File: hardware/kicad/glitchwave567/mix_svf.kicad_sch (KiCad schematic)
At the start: 50 parts, among them Q4 MMBT3904, Q5 MMBT3904, Q6 MMBT3904, U10 LM13700, U11 LM13700, U12 LM13700, U13 CD4051B, U9 TL074

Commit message: hardware: root hierarchy + ERC pass on KiCad 10 (down to lib-mismatch/footprint noise + 2 intentional OTA current-sum waivers)
- root sheet ties all 8 sheets into one project (global-label connectivity, 288 comps / 259 nets stitch verified)
- fixed: U11/U12->U18/U19 ref clash, MCU cap ref clashes, env rectifier D81 feedback returned to virtual ground (was floating FW_IN2), PWR_FLAGs on PICO_VSYS + ctrl rails, off-grid buffer pin
- remaining ERC: footprint_link (assignment pending), lib_symbol_mismatch (v6 embedded vs v10 libs, cosmetic), 2x pin_to_pin Output-Output = LM13700 current summing (by design, noted on sheets)

Co-Authored-By: Claude Fable 5 <noreply@anthropic.com>
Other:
- note added: "NOTE: U10A+U10B outputs tied = OTA CURRENT summing (intentional; ERC output-output waiver)."
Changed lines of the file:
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@@
   (no_connect (at 332.74 83.82))
   (no_connect (at 317.5 83.82))
-  (no_connect (at 317.5 108.0))
-  (no_connect (at 327.66 110.54))
+  (no_connect (at 317.5 107.95))
+  (no_connect (at 327.66 110.49))
   (no_connect (at 317.5 127.0))
   (no_connect (at 327.66 129.54))
@@
     (stroke (width 0.0))
   )
+  (text "NOTE: U10A+U10B outputs tied = OTA CURRENT summing (intentional; ERC output-output waiver)."
+    (at 25.4 33.02 0)
+    (effects (font (size 1.5 1.5)))
+  )
   (text "MIX crossfade: WET (raw 567 square) and DRY (Bazz Fuss) each through a VCA; output CURRENTS sum at U9A virtual ground (free mixing)."
     (at 25.4 25.4 0)
@@
     )
   )
-  (symbol (lib_id "Amplifier_Operational:LM13700") (at 325.12 108.0 0) (unit 2)
-    (in_bom yes) (on_board yes) (dnp no)
-    (property "Reference" "U12" (id 0) (at 325.12 105.46 0)
-      (effects (font (size 1.27 1.27)))
-    )
-    (property "Value" "LM13700" (id 1) (at 325.12 110.54 0)
-      (effects (font (size 1.27 1.27)))
-    )
-    (property "Footprint" "" (id 2) (at 325.12 108.0 0)
-      (effects (font (size 1.27 1.27)) hide)
-    )
-    (property "Datasheet" "" (id 3) (at 325.12 108.0 0)
-      (effects (font (size 1.27 1.27)) hide)
-    )
+  (symbol (lib_id "Amplifier_Operational:LM13700") (at 325.12 107.95 0) (unit 2)
+    (in_bom yes) (on_board yes) (dnp no)
+    (property "Reference" "U12" (id 0) (at 325.12 105.41 0)
+      (effects (font (size 1.27 1.27)))
+    )
+    (property "Value" "LM13700" (id 1) (at 325.12 110.49000000000001 0)
+      (effects (font (size 1.27 1.27)))
+    )
+    (property "Footprint" "" (id 2) (at 325.12 107.95 0)
+      (effects (font (size 1.27 1.27)) hide)
+    )
+    (property "Datasheet" "" (id 3) (at 325.12 107.95 0)
+      (effects (font (size 1.27 1.27)) hide)
+    )

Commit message: hardware: datasheet review pass - 13 fixes incl. 2 fatal (MP1584 pin scramble, SVF feedback dividers)
HIGH: MP1584 symbol pins remapped to real SOIC-8; EN divider 24k9 added (18V
on a 6V-max pin); SVF integrator 220k/680 feedback dividers + 220p caps
(was tuning to 611kHz); LM13700 buffer 10k DC loads; 78L09->1N4148W drop
(LM567C 9V abs max); bell EQ redesigned (was electrically inert - now exact
+3.04dB@790Hz Q=0.500); Pico ADC_VREF external feed removed (onboard ref).
MED: FREQ_CV 2nd PWM pole (-112dB, pitch FM), env attack 3.9k (exact 4ms),
567 pin3 1k clamp limit, SMAJ18A on VA, 50V input cap, buffer parking.
Full report: hardware/SCHEMATIC_REVIEW.md. All sheets re-verified.

Co-Authored-By: Claude Fable 5 <noreply@anthropic.com>
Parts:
- added R94, R96: 220k, symbol Device:R
- added R95, R97: 680, symbol Device:R
- added R98, R99: 10k (buffer DC load), symbol Device:R
- C61, C62: value 1n -> 220p
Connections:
- net GND: now also U10.10, U10.7, U12.7, R98.2, R99.2
- net SVF_BP: now also R94.1, R98.1; no longer U11.4 (-)
- net SVF_LP: now also R96.1, R99.1; no longer U11.13 (-)
- net VREF: now also R95.2, R97.2
- new net I1_M: R94.2, R95.1, U11.4 (-)
- new net I2_M: R96.2, R97.1, U11.13 (-)
- no-connect marks 18 -> 15

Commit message: hardware: footprint phase complete - 297/297 parts footprinted, custom Glitchwave.pretty authored from factory drawings
- Glitchwave.pretty: PJ-603A (pads 7.6/15.1/22.5, slots per HY-WI-32), PJ-3410,
  DC-044A (polarity DMM-verify flagged), ALPS_RK09K1130 (2.5 pitch + 8.8 snap
  legs from ALPS drawing), SSWFS-S01 (slot pads absorb 5.5-6.5 pin-spacing
  ambiguity; NOTE: PC-pin variant thread is 15/32-32 - panel hole D12.2+keyway,
  not M12), RPi_Pico_SMD (official Fig.5 land pattern, row c-c 19.38)
- schgen auto-footprint map wired into add(); all sheets regenerated
- fp-lib-tables for both projects; trims -> Bourns 3224W; clamps -> 1N5819W

Co-Authored-By: Claude Fable 5 <noreply@anthropic.com>
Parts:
- C60, C61, C62, C63, C64, C65, C66, C67: footprint (none) -> Capacitor_SMD:C_0603_1608Metric
- Q4, Q5, Q6: footprint (none) -> Package_TO_SOT_SMD:SOT-23
- R60, R61, R62, R63, R64, R65, R66, R67, R68, R69, R70, R71, R72, R73, R74, R75, R76, R77, R78, R79, R80, R81, R82, R83, R84, R85, R86, R87, R88, R89, R90, R91, R92, R93, R94, R95, R96, R97, R98, R99: footprint (none) -> Resistor_SMD:R_0603_1608Metric
- U10, U11, U12, U13: footprint (none) -> Package_SO:SOIC-16_3.9x9.9mm_P1.27mm
- U9: footprint (none) -> Package_SO:SOIC-14_3.9x8.7mm_P1.27mm

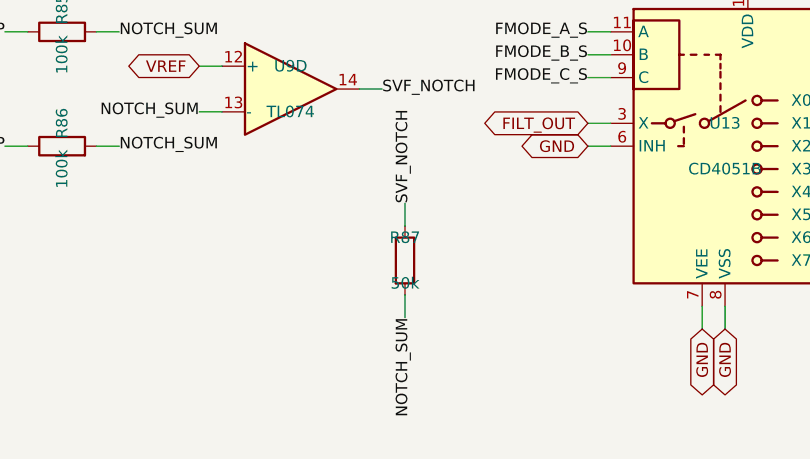
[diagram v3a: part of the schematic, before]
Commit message: hardware: turnkey BOM (319 parts, all semis verified vs live LCSC/JLC stock)
BOM.xlsx: MAIN 297 + CTRL 22 parts, grouped, LCSC C-numbers for every named
part. Highlights: LM13700MX/NOPB C174050 genuine TI x6 (5.7k stock);
MMBFJ201 C891687 genuine onsemi (EOL fear unfounded, 30k stock); LM567CMX
C18353; MP1584EN C15051 (NRND noted); CD4051/52 TI preferred-lib; Suntsu
stomps = Digi-Key line (Marketplace confirm flagged). Value fixes: 51k,
845R 1% Fetzer, inductor -> SMDRI127-220MT C9905 (12x12 fp). README sheet
carries first-article checklist.

Co-Authored-By: Claude Fable 5 <noreply@anthropic.com>
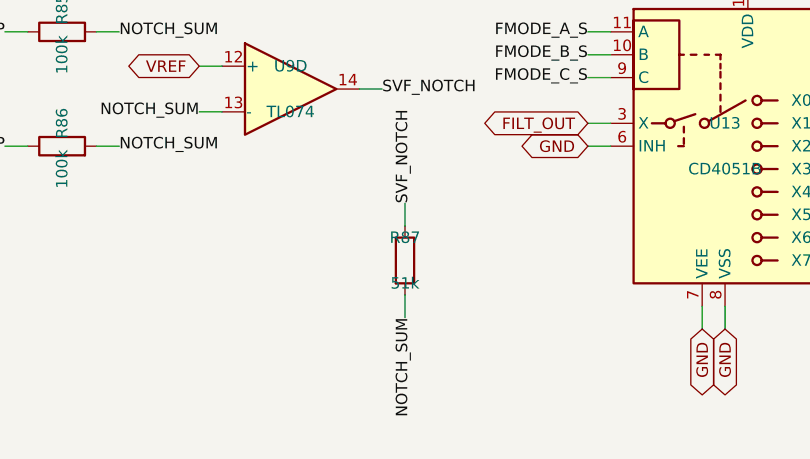
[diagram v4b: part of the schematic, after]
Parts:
- R87: value 50k -> 51k
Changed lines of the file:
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@@
       (effects (font (size 1.27 1.27)))
     )
-    (property "Value" "50k" (id 1) (at 193.04 218.44 0)
+    (property "Value" "51k" (id 1) (at 193.04 218.44 0)
       (effects (font (size 1.27 1.27)))
     )
